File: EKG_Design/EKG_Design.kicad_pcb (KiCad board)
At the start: 2 copper layers, 40.7 x 23.5 mm, 56 parts, among them IC101 OPA2156IDGKR, IC102 OPA2156IDGKR, IC103 OPA2156IDGKR, IC104 INA826AIDR_/_SOIC8, J100 Conn_01x02_Pin, J101 Conn_01x02_Pin, J102 Conn_01x02_Pin, J103 Conn_01x02_Pin, J104 Conn_01x03_Pin, Q200 BC848C

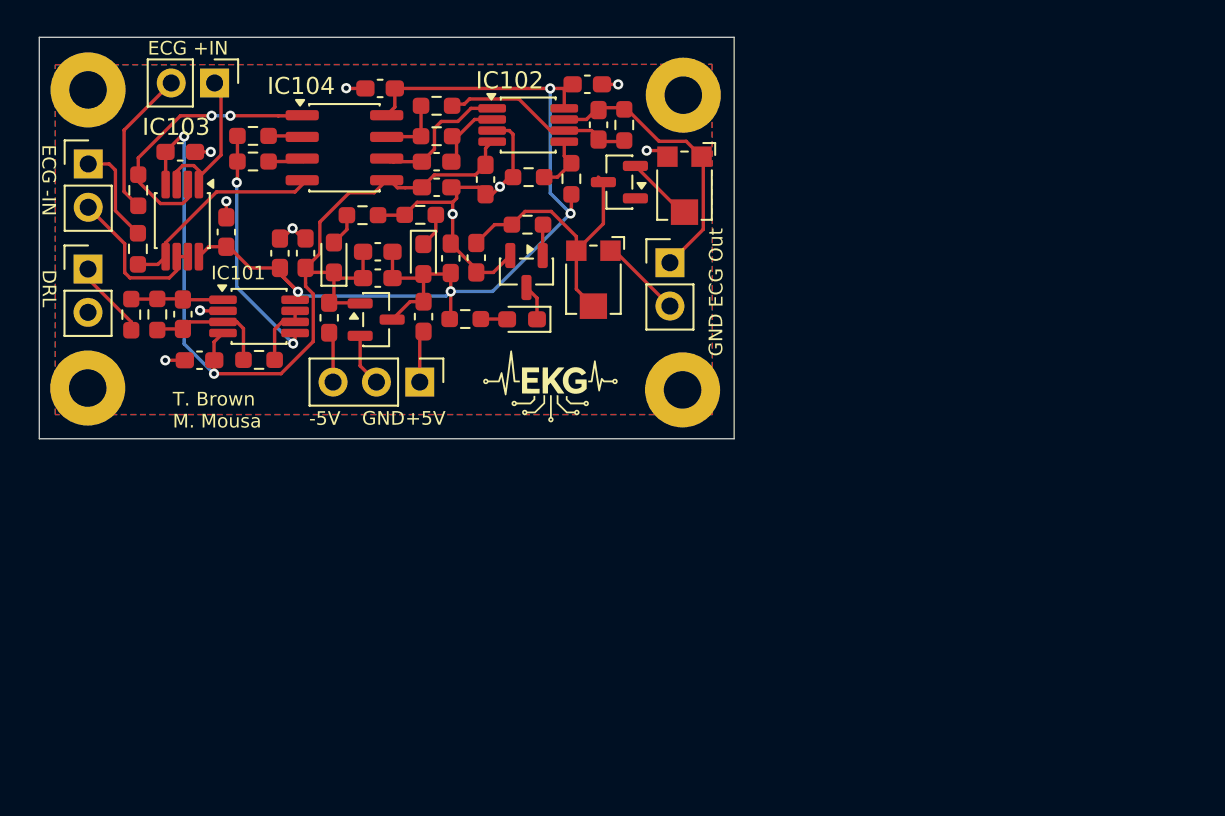
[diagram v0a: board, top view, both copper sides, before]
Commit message: Added Sheet details to info box on PCB
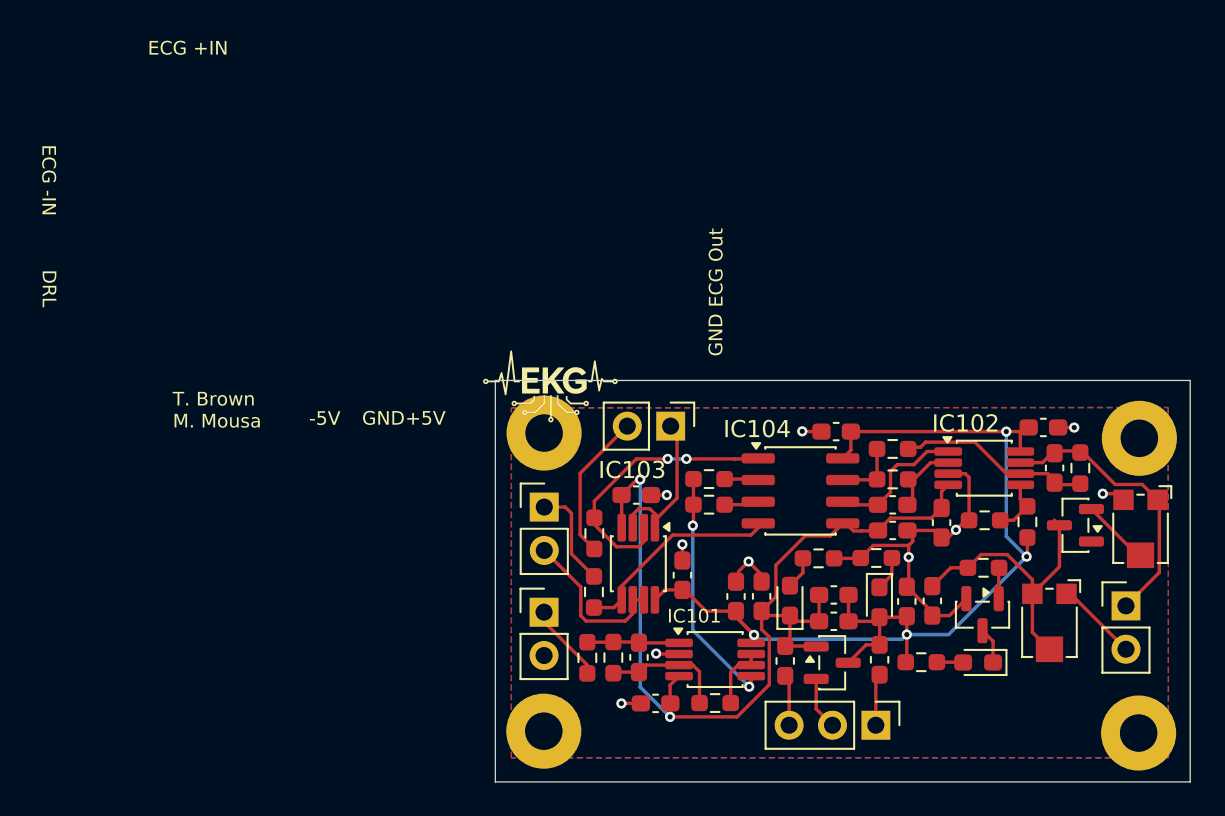
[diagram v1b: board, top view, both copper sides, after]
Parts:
- moved C101 33.4 mm to (151.6, 92.1)
- moved C102 33.4 mm to (127.2, 103.2)
- moved C103 33.4 mm to (142.9, 100.0)
- moved C106 33.4 mm to (134.4, 99.6)
- moved C109 33.4 mm to (138.6, 99.6)
- moved C200 33.4 mm to (144.4, 99.9)
- moved D101 33.4 mm to (141.3, 100.0)
- moved IC104 33.4 mm to (136.7, 93.5)
- moved J102 33.4 mm to (121.6, 100.6)
- moved R102 33.4 mm to (142.1, 91.0)
- moved R104 33.4 mm to (153.1, 92.1)
- moved R105 33.4 mm to (150.0, 95.3)
- moved R106 33.4 mm to (147.5, 95.2)
- moved R108 33.4 mm to (125.7, 103.2)
- moved R112 33.4 mm to (124.6, 96.0)
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
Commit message: fixed a new DRC error
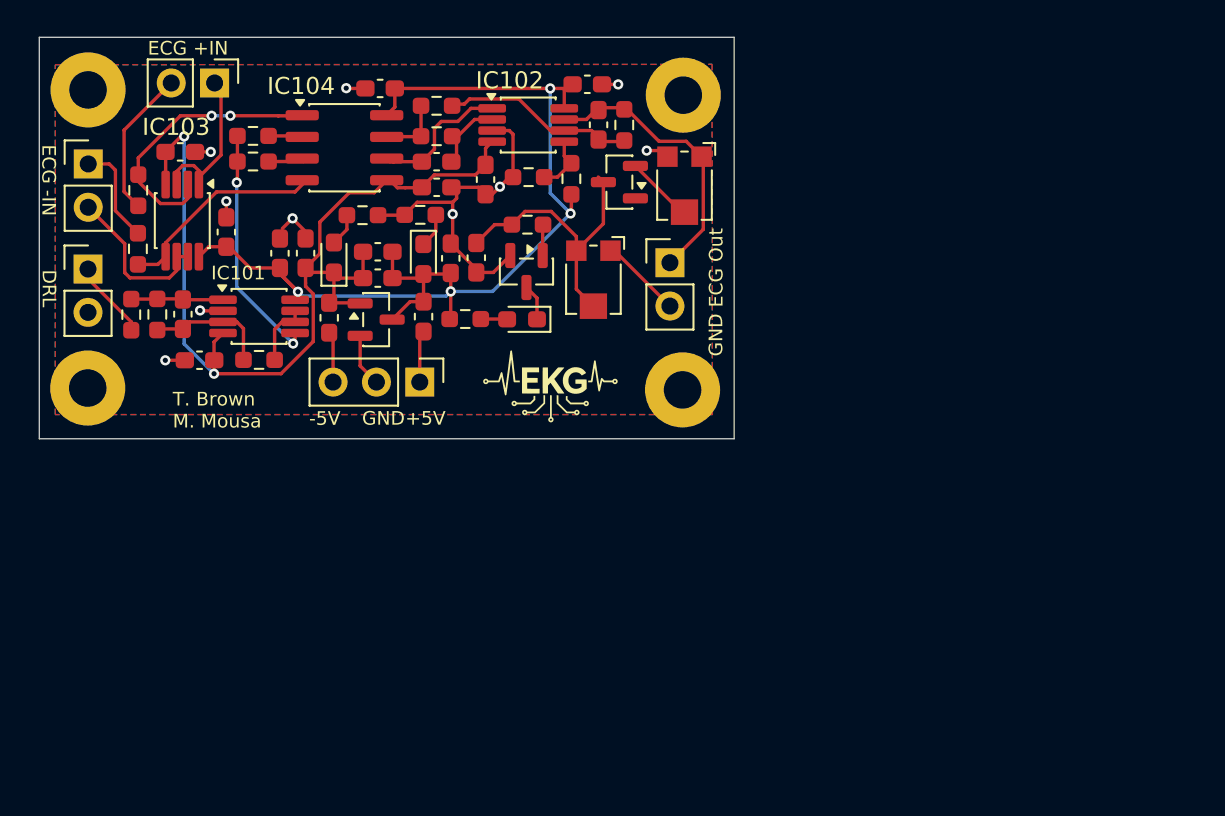
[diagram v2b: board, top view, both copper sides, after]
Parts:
- moved C101 33.4 mm to (124.8, 72.0)
- moved C102 33.4 mm to (100.5, 83.1)
- moved C103 33.4 mm to (116.2, 79.8)
- moved C106 33.4 mm to (107.7, 79.5)
- moved C109 33.4 mm to (111.9, 79.5)
- moved C200 33.4 mm to (117.7, 79.8)
- moved D101 33.4 mm to (114.6, 79.9)
- moved IC104 33.4 mm to (109.9, 73.4)
- moved J102 33.4 mm to (94.9, 80.5)
- moved R102 33.4 mm to (115.3, 70.9)
- moved R104 33.4 mm to (126.3, 72.0)
- moved R105 33.4 mm to (123.2, 75.2)
- moved R106 33.4 mm to (120.7, 75.1)
- moved R108 33.4 mm to (99.0, 83.1)
- moved R112 33.4 mm to (97.9, 75.9)
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
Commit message: fixed the remaining DRC and ERC errors
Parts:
- RV302: value 1k /25% -> 1k / 25%
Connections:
- D200 pad 1: /ECG-PulseDetection/X -> unconnected-(D200-A-Pad1)
